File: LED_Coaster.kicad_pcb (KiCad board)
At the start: 2 copper layers, 28 parts, among them U1 ATmega32U4-A

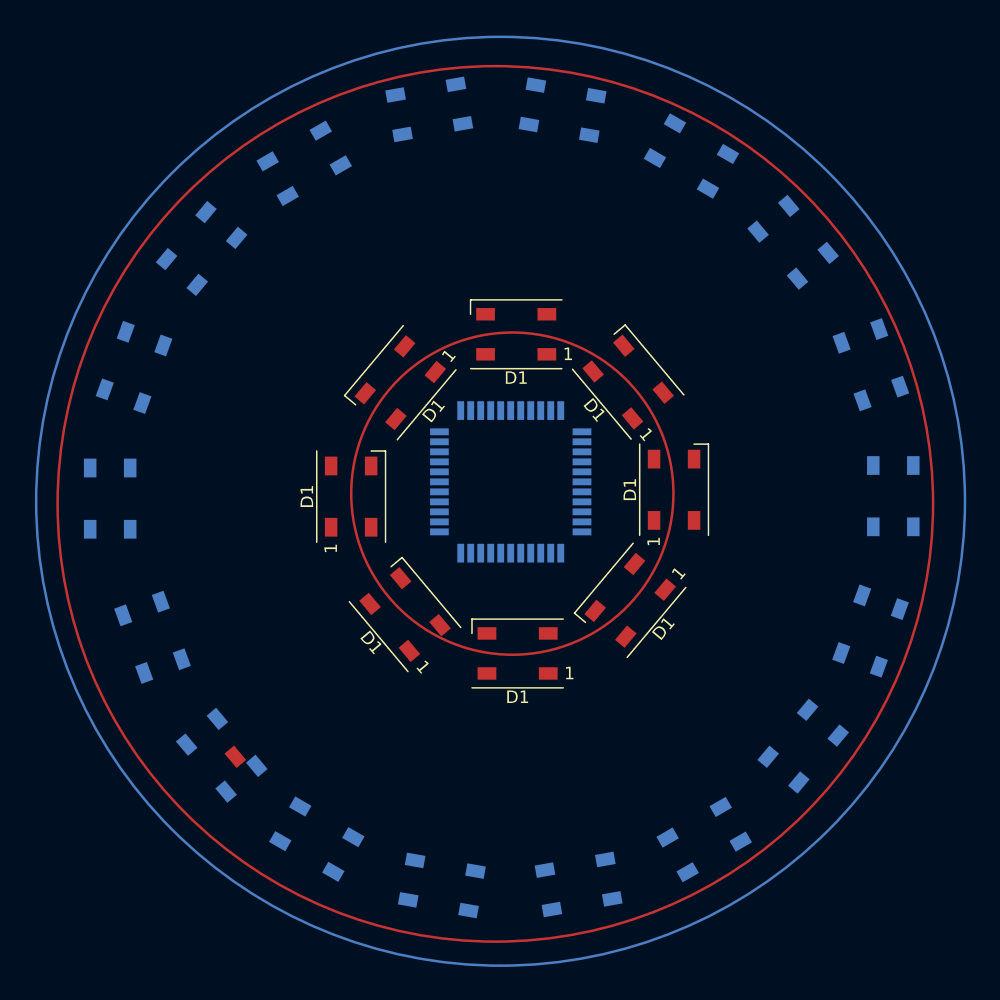
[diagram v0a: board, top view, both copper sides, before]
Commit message: Code for controlling the LED
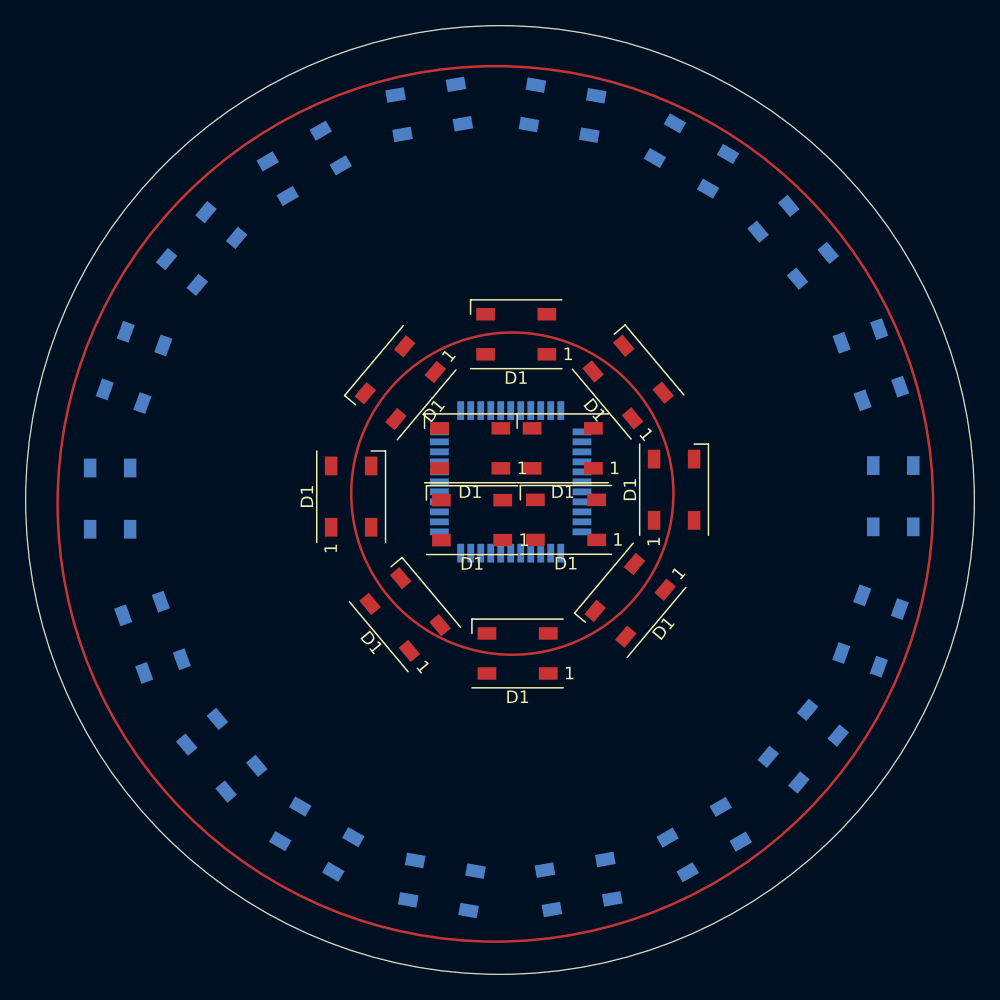
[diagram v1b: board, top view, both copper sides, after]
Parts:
- removed ?: , 
- added D1: WS2812B, LED_SMD:LED_WS2812B_PLCC4_5.0x5.0mm_P3.2mm, F.Cu at (76.7, 88.1)
- added D1: WS2812B, LED_SMD:LED_WS2812B_PLCC4_5.0x5.0mm_P3.2mm, F.Cu at (76.5, 82.3)
- added D1: WS2812B, LED_SMD:LED_WS2812B_PLCC4_5.0x5.0mm_P3.2mm, F.Cu at (83.9, 82.3)
- added D1: WS2812B, LED_SMD:LED_WS2812B_PLCC4_5.0x5.0mm_P3.2mm, F.Cu at (84.2, 88.0)
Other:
- board outline added: 75.9 x 75.9 mm

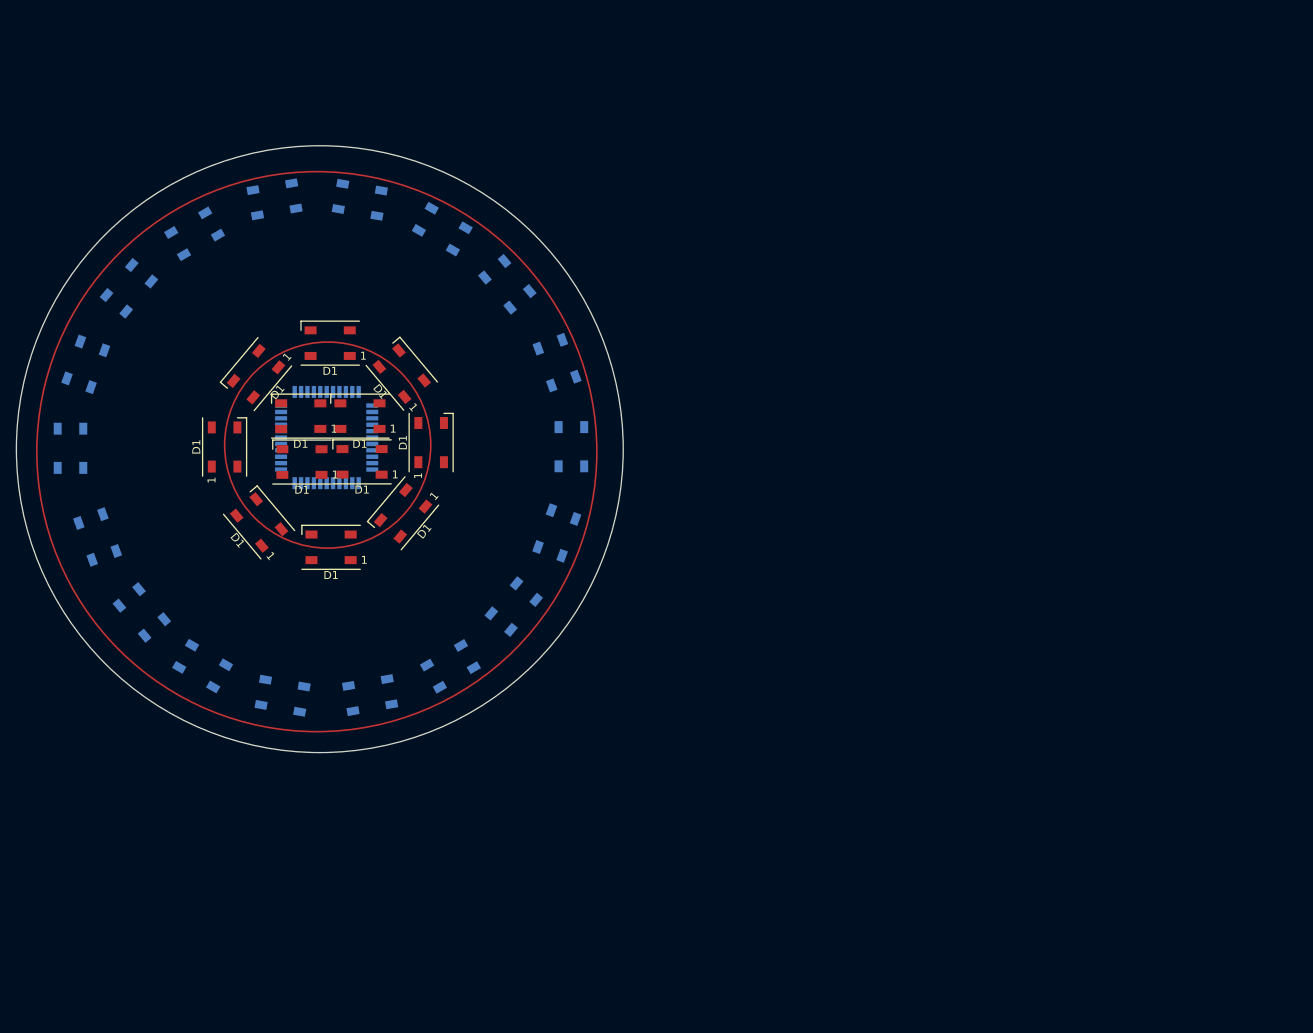
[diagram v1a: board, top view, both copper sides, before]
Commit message: Added outer ring of LEDs
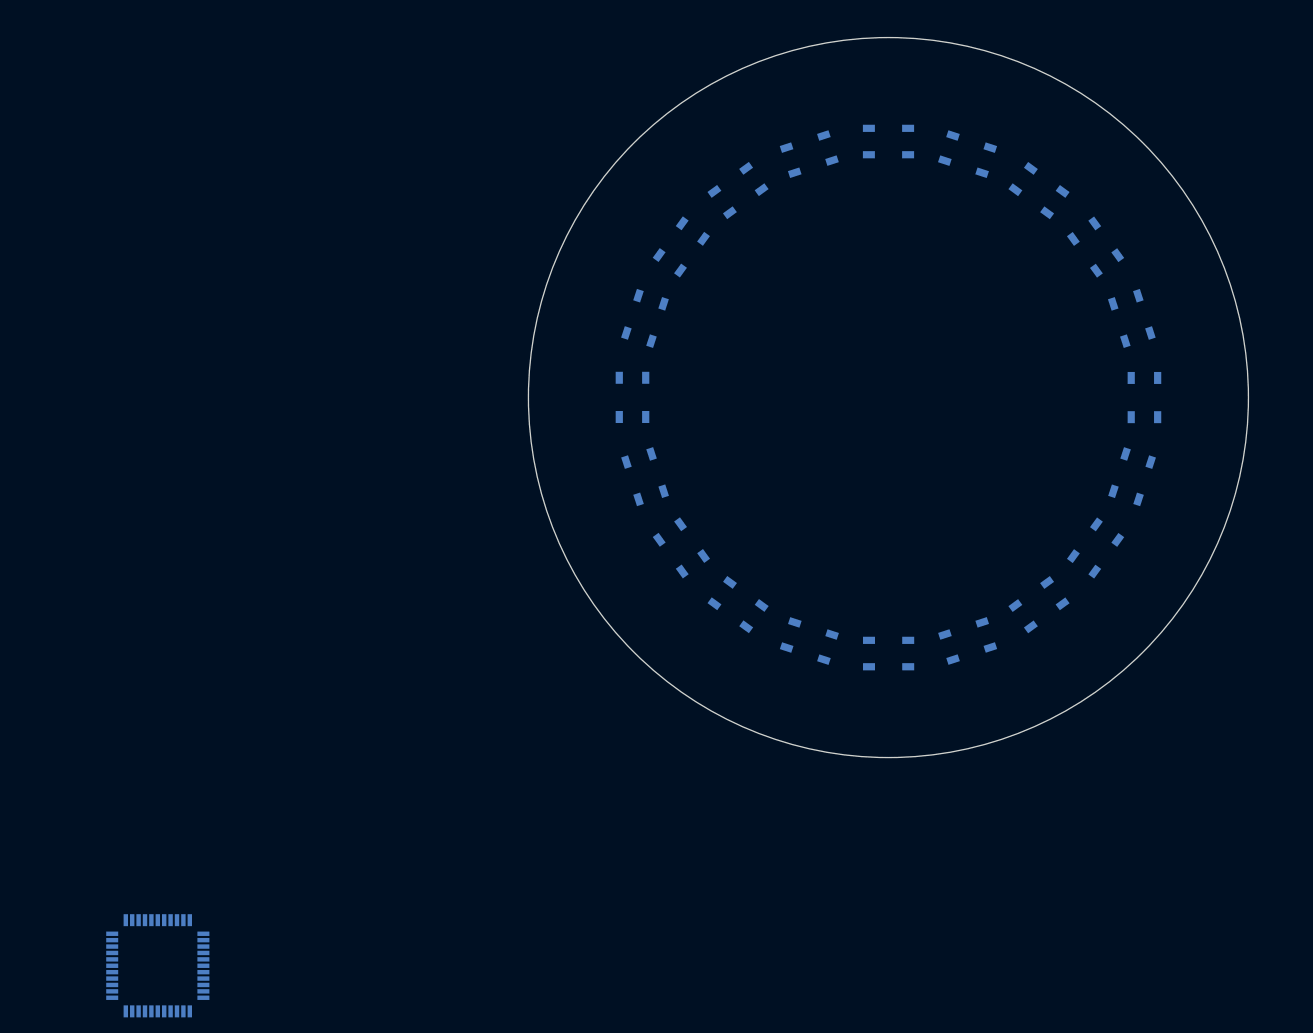
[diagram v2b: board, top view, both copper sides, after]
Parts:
- removed the D1 at (80.3, 98.7)
- removed the D1 at (76.7, 88.1)
- removed the D1 at (80.2, 73.2)
- removed the D1 at (71.0, 77.1)
- removed the D1 at (102.4, 65.8)
- removed the D1 at (51.1, 97.4)
- removed the D1 at (103.2, 106.1)
- removed the D1 at (110.4, 86.1)
- removed the D1 at (56.7, 106.9)
- removed the D1 at (47.8, 86.3)
- removed the D1 at (85.2, 117.2)
- removed the D1 at (92.8, 85.6)
- removed the D1 at (73.3, 55.2)
- removed the D1 at (64.3, 113.6)
- removed the D1 at (95.2, 113.6)
- removed the D1 at (83.9, 55.3)
- removed the D1 at (49.7, 75.8)
- removed the D1 at (108.6, 75.6)
- removed the D1 at (55.1, 66.3)
- removed the D1 at (63.3, 59.5)
- removed the D1 at (74.3, 117.3)
- removed the D1 at (94.2, 58.9)
- removed the D1 at (71.3, 95.6)
- removed the D1 at (108.5, 96.9)
- removed the D1 at (89.3, 94.5)
- removed the D1 at (76.5, 82.3)
- removed the D1 at (89.2, 77.0)
- removed the D1 at (83.9, 82.3)
- removed the D1 at (67.0, 86.2)
- removed the D1 at (84.2, 88.0)
- added D1: WS2812B, LED_SMD:LED_WS2812B_PLCC4_5.0x5.0mm_P3.2mm, B.Cu at (182.0, 80.0)
- added D10: WS2812B, LED_SMD:LED_WS2812B_PLCC4_5.0x5.0mm_P3.2mm, B.Cu at (119.6, 70.1)
- added D11: WS2812B, LED_SMD:LED_WS2812B_PLCC4_5.0x5.0mm_P3.2mm, B.Cu at (118.0, 80.0)
- added D12: WS2812B, LED_SMD:LED_WS2812B_PLCC4_5.0x5.0mm_P3.2mm, B.Cu at (119.6, 89.9)
- added D13: WS2812B, LED_SMD:LED_WS2812B_PLCC4_5.0x5.0mm_P3.2mm, B.Cu at (124.1, 98.8)
- added D14: WS2812B, LED_SMD:LED_WS2812B_PLCC4_5.0x5.0mm_P3.2mm, B.Cu at (131.2, 105.9)
- added D15: WS2812B, LED_SMD:LED_WS2812B_PLCC4_5.0x5.0mm_P3.2mm, B.Cu at (140.1, 110.4)
- added D16: WS2812B, LED_SMD:LED_WS2812B_PLCC4_5.0x5.0mm_P3.2mm, B.Cu at (150.0, 112.0)
- added D17: WS2812B, LED_SMD:LED_WS2812B_PLCC4_5.0x5.0mm_P3.2mm, B.Cu at (159.9, 110.4)
- added D18: WS2812B, LED_SMD:LED_WS2812B_PLCC4_5.0x5.0mm_P3.2mm, B.Cu at (168.8, 105.9)
- added D19: WS2812B, LED_SMD:LED_WS2812B_PLCC4_5.0x5.0mm_P3.2mm, B.Cu at (175.9, 98.8)
- added D2: WS2812B, LED_SMD:LED_WS2812B_PLCC4_5.0x5.0mm_P3.2mm, B.Cu at (180.4, 70.1)
- added D20: WS2812B, LED_SMD:LED_WS2812B_PLCC4_5.0x5.0mm_P3.2mm, B.Cu at (180.5, 89.9)
- added D3: WS2812B, LED_SMD:LED_WS2812B_PLCC4_5.0x5.0mm_P3.2mm, B.Cu at (175.9, 61.2)
- added D4: WS2812B, LED_SMD:LED_WS2812B_PLCC4_5.0x5.0mm_P3.2mm, B.Cu at (168.8, 54.1)
- added D5: WS2812B, LED_SMD:LED_WS2812B_PLCC4_5.0x5.0mm_P3.2mm, B.Cu at (159.9, 49.6)
- added D6: WS2812B, LED_SMD:LED_WS2812B_PLCC4_5.0x5.0mm_P3.2mm, B.Cu at (150.0, 48.0)
- added D7: WS2812B, LED_SMD:LED_WS2812B_PLCC4_5.0x5.0mm_P3.2mm, B.Cu at (140.1, 49.6)
- added D8: WS2812B, LED_SMD:LED_WS2812B_PLCC4_5.0x5.0mm_P3.2mm, B.Cu at (131.2, 54.1)
- added D9: WS2812B, LED_SMD:LED_WS2812B_PLCC4_5.0x5.0mm_P3.2mm, B.Cu at (124.1, 61.2)
- moved U1 69.3 mm to (58.7, 151.0)
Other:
- board size 75.9 x 75.9 mm -> 90 x 90 mm

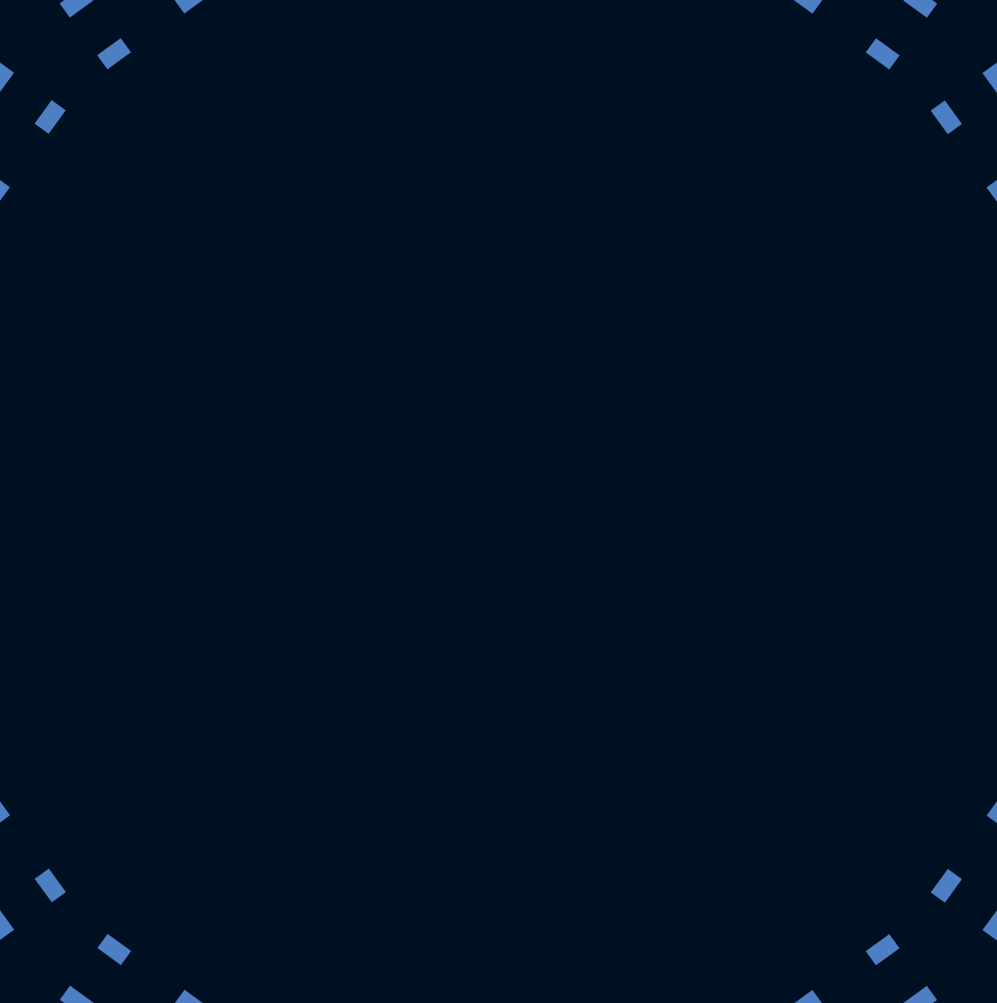
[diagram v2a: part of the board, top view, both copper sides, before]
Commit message: Added inner ring of LEDs
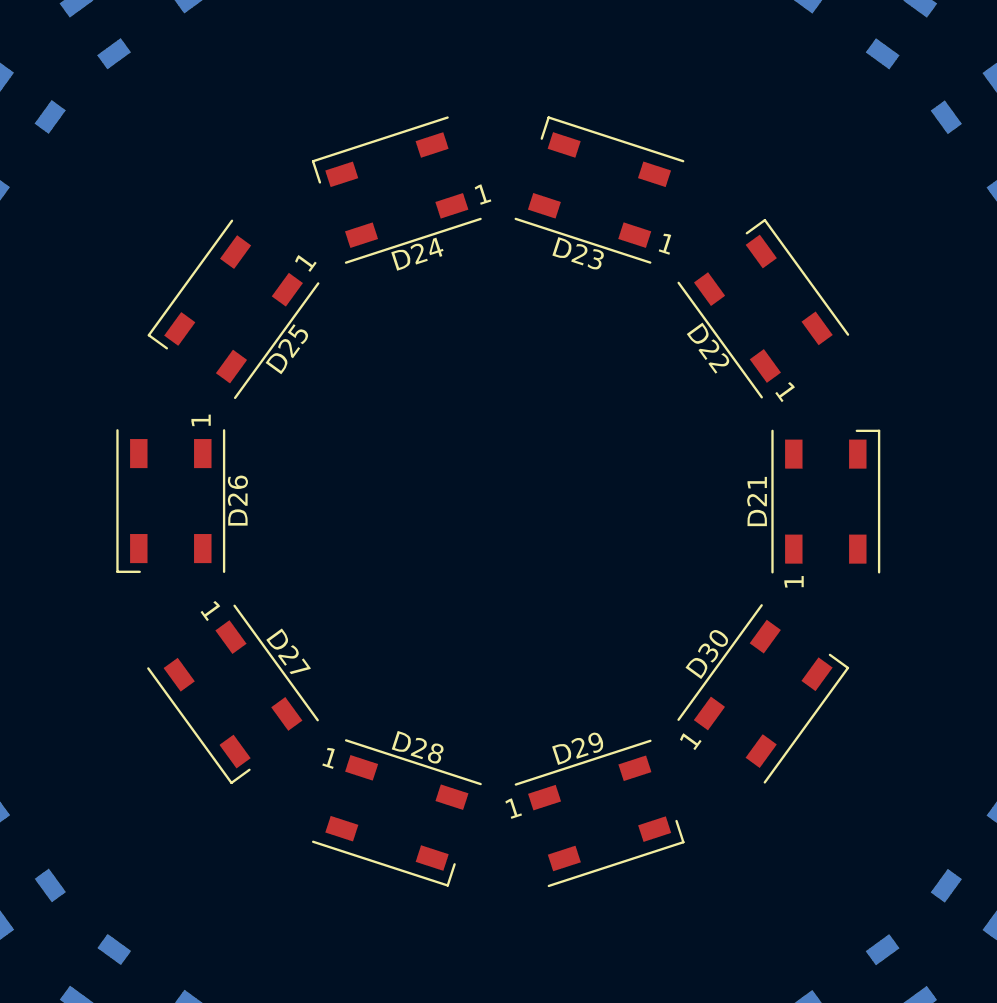
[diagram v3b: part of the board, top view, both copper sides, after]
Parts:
- added D21: WS2812B, LED_SMD:LED_WS2812B_PLCC4_5.0x5.0mm_P3.2mm, F.Cu at (166.9, 80.0)
- added D22: WS2812B, LED_SMD:LED_WS2812B_PLCC4_5.0x5.0mm_P3.2mm, F.Cu at (163.7, 70.1)
- added D23: WS2812B, LED_SMD:LED_WS2812B_PLCC4_5.0x5.0mm_P3.2mm, F.Cu at (155.2, 63.9)
- added D24: WS2812B, LED_SMD:LED_WS2812B_PLCC4_5.0x5.0mm_P3.2mm, F.Cu at (144.8, 63.9)
- added D25: WS2812B, LED_SMD:LED_WS2812B_PLCC4_5.0x5.0mm_P3.2mm, F.Cu at (136.3, 70.1)
- added D26: WS2812B, LED_SMD:LED_WS2812B_PLCC4_5.0x5.0mm_P3.2mm, F.Cu at (133.1, 80.0)
- added D27: WS2812B, LED_SMD:LED_WS2812B_PLCC4_5.0x5.0mm_P3.2mm, F.Cu at (136.3, 89.9)
- added D28: WS2812B, LED_SMD:LED_WS2812B_PLCC4_5.0x5.0mm_P3.2mm, F.Cu at (144.8, 96.1)
- added D29: WS2812B, LED_SMD:LED_WS2812B_PLCC4_5.0x5.0mm_P3.2mm, F.Cu at (155.2, 96.1)
- added D30: WS2812B, LED_SMD:LED_WS2812B_PLCC4_5.0x5.0mm_P3.2mm, F.Cu at (163.7, 89.9)

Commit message: MCU schematic halfway done
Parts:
- added C1: 1uF, Capacitor_SMD:C_0805_2012Metric_Pad1.18x1.45mm_HandSolder, B.Cu at (199.4, 114.0)
- added C2: 10uF, Capacitor_SMD:C_0805_2012Metric_Pad1.18x1.45mm_HandSolder, B.Cu at (199.4, 117.1)
- added C3: 0.1uF, Capacitor_SMD:C_0805_2012Metric_Pad1.18x1.45mm_HandSolder, B.Cu at (199.4, 120.1)
- added C4: 0.1uF, Capacitor_SMD:C_0805_2012Metric_Pad1.18x1.45mm_HandSolder, B.Cu at (199.4, 123.1)
- added C5: 0.1uF, Capacitor_SMD:C_0805_2012Metric_Pad1.18x1.45mm_HandSolder, B.Cu at (199.4, 126.1)
- added C6: 22pF, Capacitor_SMD:C_0805_2012Metric_Pad1.18x1.45mm_HandSolder, B.Cu at (199.4, 129.1)
- added C7: 22pF, Capacitor_SMD:C_0805_2012Metric_Pad1.18x1.45mm_HandSolder, B.Cu at (199.4, 132.1)
- added J1: USB_C_Receptacle_USB2.0, Connector_USB:USB_C_Receptacle_HRO_TYPE-C-31-M-12, F.Cu at (192.1, 80.0)
- added R1: 10K, Resistor_SMD:R_0805_2012Metric_Pad1.20x1.40mm_HandSolder, B.Cu at (194.6, 114.0)
- added R2: 22, Resistor_SMD:R_0805_2012Metric_Pad1.20x1.40mm_HandSolder, B.Cu at (194.6, 117.0)
- added R3: 22, Resistor_SMD:R_0805_2012Metric_Pad1.20x1.40mm_HandSolder, B.Cu at (194.6, 119.9)
- added R4: 10K, Resistor_SMD:R_0805_2012Metric_Pad1.20x1.40mm_HandSolder, B.Cu at (194.6, 122.9)
- added SW1: SW_Push, Button_Switch_SMD:SW_SPST_SKQG_WithoutStem, F.Cu at (189.5, 69.8)
- added Y1: Crystal_GND24, Crystal:Crystal_SMD_3225-4Pin_3.2x2.5mm_HandSoldering, B.Cu at (193.2, 127.7)
- moved U1 115.7 mm to (150.0, 80.0)
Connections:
- U1 pad 13: unconnected-(U1-~{RESET}-Pad13) -> Net-(U1-~{RESET})
- U1 pad 14: Net-(U1-VCC-Pad14) -> +5V
- U1 pad 15: Net-(U1-GND-Pad15) -> GND
- U1 pad 16: unconnected-(U1-XTAL2-Pad16) -> Net-(U1-XTAL2)
- U1 pad 17: unconnected-(U1-XTAL1-Pad17) -> Net-(U1-XTAL1)
- U1 pad 2: unconnected-(U1-UVCC-Pad2) -> +5V
- U1 pad 23: Net-(U1-GND-Pad15) -> GND
- U1 pad 24: Net-(U1-AVCC-Pad24) -> +5V
- U1 pad 3: unconnected-(U1-D--Pad3) -> Net-(U1-D-)
- U1 pad 33: unconnected-(U1-~{HWB}/PE2-Pad33) -> Net-(U1-~{HWB}/PE2)
- U1 pad 34: Net-(U1-VCC-Pad14) -> +5V
- U1 pad 35: Net-(U1-GND-Pad15) -> GND
- U1 pad 4: unconnected-(U1-D+-Pad4) -> Net-(U1-D+)
- U1 pad 43: Net-(U1-GND-Pad15) -> GND
- U1 pad 44: Net-(U1-AVCC-Pad24) -> +5V
- U1 pad 5: unconnected-(U1-UGND-Pad5) -> GND
- U1 pad 6: unconnected-(U1-UCAP-Pad6) -> Net-(U1-UCAP)
- U1 pad 7: unconnected-(U1-VBUS-Pad7) -> +5V
